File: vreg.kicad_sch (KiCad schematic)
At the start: 24 parts, among them IC9 LTC3113, J5 MMCX-P-P-H-ST-TH1

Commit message: name change to Loriques
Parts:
- C10, C11, C24, C69, C75: symbol autonode:CAP0402 -> Loriques:CAP0402
- C28, C32: symbol autonode:CAP -> Loriques:CAP
- C33, C38: symbol autonode:CAP0603 -> Loriques:CAP0603
- C41, C45, C46: symbol autonode:CAP1206 -> Loriques:CAP1206
- COVER0: footprint autonode:NOTHING -> Loriques:NOTHING; symbol autonode:BULLET -> Loriques:BULLET
- FL1: footprint autonode:YFF31HC2A104MT000N -> Loriques:YFF31HC2A104MT000N; symbol autonode:YFF31HC2A104MT000N -> Loriques:YFF31HC2A104MT000N
- IC9: footprint autonode:SON50P400X500X80-17T244X434N -> Loriques:SON50P400X500X80-17T244X434N; symbol autonode:LTC3113 -> Loriques:LTC3113
- J5: footprint autonode:MMCX-P-P-H-ST-TH1 -> Loriques:MMCX-P-P-H-ST-TH1; symbol autonode:MMCX-P-P-H-ST-TH1 -> Loriques:MMCX-P-P-H-ST-TH1
- L1: footprint autonode:HCMA0703-2R2-R -> Loriques:HCMA0703-2R2-R; symbol autonode:HCMA0703-2R2-R -> Loriques:HCMA0703-2R2-R
- R3, R34, R35, R39, R6, R7: symbol autonode:RESISTOR0402-RES -> Loriques:RESISTOR0402-RES
- S1: footprint autonode:MS288-10F -> Loriques:MS288-10F; symbol autonode:MS288-10F -> Loriques:MS288-10F
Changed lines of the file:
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@@
 	)
 	(symbol
-		(lib_id "autonode:CAP1206")
+		(lib_id "Loriques:CAP1206")
 		(at 88.9 104.14 0)
 		(unit 1)
@@
 		)
 		(instances
-			(project "AutoNode"
+			(project "Loriques"
 				(path "/23714a9e-6212-41ed-9d80-e983f828d45f/a02f1723-ba56-4604-a65b-8dc913c22eb2"
 					(reference "C46")
@@
 	)
 	(symbol
-		(lib_id "autonode:RESISTOR0402-RES")
+		(lib_id "Loriques:RESISTOR0402-RES")
 		(at 256.54 83.82 90)
 		(unit 1)
@@
 		)
 		(instances
-			(project "AutoNode"
+			(project "Loriques"
 				(path "/23714a9e-6212-41ed-9d80-e983f828d45f/a02f1723-ba56-4604-a65b-8dc913c22eb2"
 					(reference "R6")
@@
 	)
 	(symbol
-		(lib_id "autonode:CAP0402")
+		(lib_id "Loriques:CAP0402")
 		(at 228.6 78.74 0)
 		(unit 1)
@@
 		)
 		(instances
-			(project "AutoNode"
+			(project "Loriques"
 				(path "/23714a9e-6212-41ed-9d80-e983f828d45f/a02f1723-ba56-4604-a65b-8dc913c22eb2"
 					(reference "C10")
@@
 	)
 	(symbol
-		(lib_id "autonode:RESISTOR0402-RES")
+		(lib_id "Loriques:RESISTOR0402-RES")
 		(at 170.18 93.98 90)
 		(unit 1)
@@
 		)
 		(instances
-			(project "AutoNode"
+			(project "Loriques"
 				(path "/23714a9e-6212-41ed-9d80-e983f828d45f/a02f1723-ba56-4604-a65b-8dc913c22eb2"
 					(reference "R39")
@@
 	)
 	(symbol
-		(lib_id "autonode:YFF31HC2A104MT000N")
+		(lib_id "Loriques:YFF31HC2A104MT000N")
 		(at 50.8 86.36 0)
 		(unit 1)
@@
 			)
 		)
-		(property "Footprint" "autonode:YFF31HC2A104MT000N"
+		(property "Footprint" "Loriques:YFF31HC2A104MT000N"
 			(at 50.8 86.36 0)
 			(effects
@@
 		)
 		(instances
-			(project "AutoNode"
+			(project "Loriques"
 				(path "/23714a9e-6212-41ed-9d80-e983f828d45f/a02f1723-ba56-4604-a65b-8dc913c22eb2"
 					(reference "FL1")
@@
 	)
 	(symbol
-		(lib_id "autonode:CAP")
+		(lib_id "Loriques:CAP")
 		(at 142.24 104.14 0)
 		(unit 1)
@@
 		)
 		(instances
-			(project "AutoNode"
+			(project "Loriques"
 				(path "/23714a9e-6212-41ed-9d80-e983f828d45f/a02f1723-ba56-4604-a65b-8dc913c22eb2"
 					(reference "C28")
@@
 	)
 	(symbol
-		(lib_id "autonode:CAP0402")
+		(lib_id "Loriques:CAP0402")
 		(at 246.38 101.6 90)
 		(unit 1)
@@
 		)
 		(instances
-			(project "AutoNode"
+			(project "Loriques"
 				(path "/23714a9e-6212-41ed-9d80-e983f828d45f/a02f1723-ba56-4604-a65b-8dc913c22eb2"
 					(reference "C24")
@@
 	)
 	(symbol
-		(lib_id "autonode:CAP0402")
+		(lib_id "Loriques:CAP0402")
 		(at 132.08 104.14 0)
 		(unit 1)
@@
 		)
 		(instances
-			(project "AutoNode"
+			(project "Loriques"
 				(path "/23714a9e-6212-41ed-9d80-e983f828d45f/a02f1723-ba56-4604-a65b-8dc913c22eb2"
 					(reference "C75")
@@
 	)
 	(symbol
-		(lib_id "autonode:BULLET")
+		(lib_id "Loriques:BULLET")
 		(at 284.48 134.62 0)
 		(unit 1)
@@
 			)
 		)
-		(property "Footprint" "autonode:NOTHING"
+		(property "Footprint" "Loriques:NOTHING"
 			(at 284.48 134.62 0)
 			(effects
@@
 		)
 		(instances
-			(project "AutoNode"
+			(project "Loriques"
 				(path "/23714a9e-6212-41ed-9d80-e983f828d45f/a02f1723-ba56-4604-a65b-8dc913c22eb2"
 					(reference "COVER0")
@@
 	)
 	(symbol
-		(lib_id "autonode:MMCX-P-P-H-ST-TH1")
+		(lib_id "Loriques:MMCX-P-P-H-ST-TH1")
 		(at 27.94 99.06 0)
 		(unit 1)
@@
 			)
 		)
-		(property "Footprint" "autonode:MMCX-P-P-H-ST-TH1"
+		(property "Footprint" "Loriques:MMCX-P-P-H-ST-TH1"
 			(at 27.94 99.06 0)
 			(effects
@@
 		)
 		(instances
-			(project "AutoNode"
+			(project "Loriques"
 				(path "/23714a9e-6212-41ed-9d80-e983f828d45f/a02f1723-ba56-4604-a65b-8dc913c22eb2"
 					(reference "J5")
@@
 	)
 	(symbol
-		(lib_id "autonode:LTC3113")
+		(lib_id "Loriques:LTC3113")
 		(at 198.12 96.52 0)
 		(unit 1)
@@
 			)
 		)
-		(property "Footprint" "autonode:SON50P400X500X80-17T244X434N"
+		(property "Footprint" "Loriques:SON50P400X500X80-17T244X434N"
 			(at 197.866 114.554 0)
 			(effects
@@
 		)
 		(instances
-			(project "AutoNode"
+			(project "Loriques"
 				(path "/23714a9e-6212-41ed-9d80-e983f828d45f/a02f1723-ba56-4604-a65b-8dc913c22eb2"
 					(reference "IC9")
@@
 	)
 	(symbol
-		(lib_id "autonode:HCMA0703-2R2-R")
+		(lib_id "Loriques:HCMA0703-2R2-R")
 		(at 198.12 76.2 0)
 		(unit 1)
@@
 			)
 		)
-		(property "Footprint" "autonode:HCMA0703-2R2-R"
+		(property "Footprint" "Loriques:HCMA0703-2R2-R"
 			(at 198.12 76.2 0)
 			(effects
@@
 		)
 		(instances
-			(project "AutoNode"
+			(project "Loriques"
 				(path "/23714a9e-6212-41ed-9d80-e983f828d45f/a02f1723-ba56-4604-a65b-8dc913c22eb2"
 					(reference "L1")
@@
 	)
 	(symbol
-		(lib_id "autonode:CAP0603")
+		(lib_id "Loriques:CAP0603")
 		(at 287.02 96.52 0)
 		(unit 1)
@@
 		)
 		(instances
-			(project "AutoNode"
+			(project "Loriques"
 				(path "/23714a9e-6212-41ed-9d80-e983f828d45f/a02f1723-ba56-4604-a65b-8dc913c22eb2"
 					(reference "C38")
@@
 	)
 	(symbol
-		(lib_id "autonode:RESISTOR0402-RES")
+		(lib_id "Loriques:RESISTOR0402-RES")
 		(at 228.6 88.9 90)
 		(unit 1)
@@
 		)
 		(instances
-			(project "AutoNode"
+			(project "Loriques"
 				(path "/23714a9e-6212-41ed-9d80-e983f828d45f/a02f1723-ba56-4604-a65b-8dc913c22eb2"
 					(reference "R3")
@@
 	)
 	(symbol
-		(lib_id "autonode:RESISTOR0402-RES")
+		(lib_id "Loriques:RESISTOR0402-RES")
 		(at 180.34 114.3 90)
 		(unit 1)
@@
 		)
 		(instances
-			(project "AutoNode"
+			(project "Loriques"
 				(path "/23714a9e-6212-41ed-9d80-e983f828d45f/a02f1723-ba56-4604-a65b-8dc913c22eb2"
 					(reference "R34")
@@
 	)
 	(symbol
-		(lib_id "autonode:CAP1206")
+		(lib_id "Loriques:CAP1206")
 		(at 63.5 104.14 0)
 		(unit 1)
@@
 		)
 		(instances
-			(project "AutoNode"
+			(project "Loriques"
 				(path "/23714a9e-6212-41ed-9d80-e983f828d45f/a02f1723-ba56-4604-a65b-8dc913c22eb2"
 					(reference "C41")
@@
 	)
 	(symbol
-		(lib_id "autonode:RESISTOR0402-RES")
+		(lib_id "Loriques:RESISTOR0402-RES")
 		(at 223.52 101.6 180)
 		(unit 1)
@@
 		)
 		(instances
-			(project "AutoNode"
+			(project "Loriques"
 				(path "/23714a9e-6212-41ed-9d80-e983f828d45f/a02f1723-ba56-4604-a65b-8dc913c22eb2"
 					(reference "R7")
@@
 	)
 	(symbol
-		(lib_id "autonode:MS288-10F")
+		(lib_id "Loriques:MS288-10F")
 		(at 294.64 127 180)
 		(unit 1)
@@
 			)
 		)
-		(property "Footprint" "autonode:MS288-10F"
+		(property "Footprint" "Loriques:MS288-10F"
 			(at 294.64 127 0)
 			(effects
@@
 		)
 		(instances
-			(project "AutoNode"
+			(project "Loriques"
 				(path "/23714a9e-6212-41ed-9d80-e983f828d45f/a02f1723-ba56-4604-a65b-8dc913c22eb2"
 					(reference "S1")
@@
 	)
 	(symbol
-		(lib_id "autonode:CAP0402")
+		(lib_id "Loriques:CAP0402")
 		(at 236.22 106.68 90)
 		(unit 1)
@@
 		)
 		(instances
-			(project "AutoNode"
+			(project "Loriques"
 				(path "/23714a9e-6212-41ed-9d80-e983f828d45f/a02f1723-ba56-4604-a65b-8dc913c22eb2"
 					(reference "C11")
@@
 	)
 	(symbol
-		(lib_id "autonode:CAP0402")
+		(lib_id "Loriques:CAP0402")
 		(at 101.6 104.14 0)
 		(unit 1)
@@
 		)
 		(instances
-			(project "AutoNode"
+			(project "Loriques"
 				(path "/23714a9e-6212-41ed-9d80-e983f828d45f/a02f1723-ba56-4604-a65b-8dc913c22eb2"
 					(reference "C69")
@@
 	)
 	(symbol
-		(lib_id "autonode:CAP")
+		(lib_id "Loriques:CAP")
 		(at 266.7 96.52 0)
 		(unit 1)
@@
 		)
 		(instances
-			(project "AutoNode"
+			(project "Loriques"
 				(path "/23714a9e-6212-41ed-9d80-e983f828d45f/a02f1723-ba56-4604-a65b-8dc913c22eb2"
 					(reference "C32")
@@
 	)
 	(symbol
-		(lib_id "autonode:RESISTOR0402-RES")
+		(lib_id "Loriques:RESISTOR0402-RES")
 		(at 256.54 114.3 90)
 		(unit 1)
@@
 		)
 		(instances
-			(project "AutoNode"
+			(project "Loriques"
 				(path "/23714a9e-6212-41ed-9d80-e983f828d45f/a02f1723-ba56-4604-a65b-8dc913c22eb2"
 					(reference "R35")
@@
 	)
 	(symbol
-		(lib_id "autonode:CAP1206")
+		(lib_id "Loriques:CAP1206")
 		(at 76.2 104.14 0)
 		(unit 1)
@@
 		)
 		(instances
-			(project "AutoNode"
+			(project "Loriques"
 				(path "/23714a9e-6212-41ed-9d80-e983f828d45f/a02f1723-ba56-4604-a65b-8dc913c22eb2"
 					(reference "C45")
@@
 	)
 	(symbol
-		(lib_id "autonode:CAP0603")
+		(lib_id "Loriques:CAP0603")
 		(at 160.02 104.14 0)
 		(unit 1)
@@
 		)
 		(instances
-			(project "AutoNode"
+			(project "Loriques"
 				(path "/23714a9e-6212-41ed-9d80-e983f828d45f/a02f1723-ba56-4604-a65b-8dc913c22eb2"
 					(reference "C33")

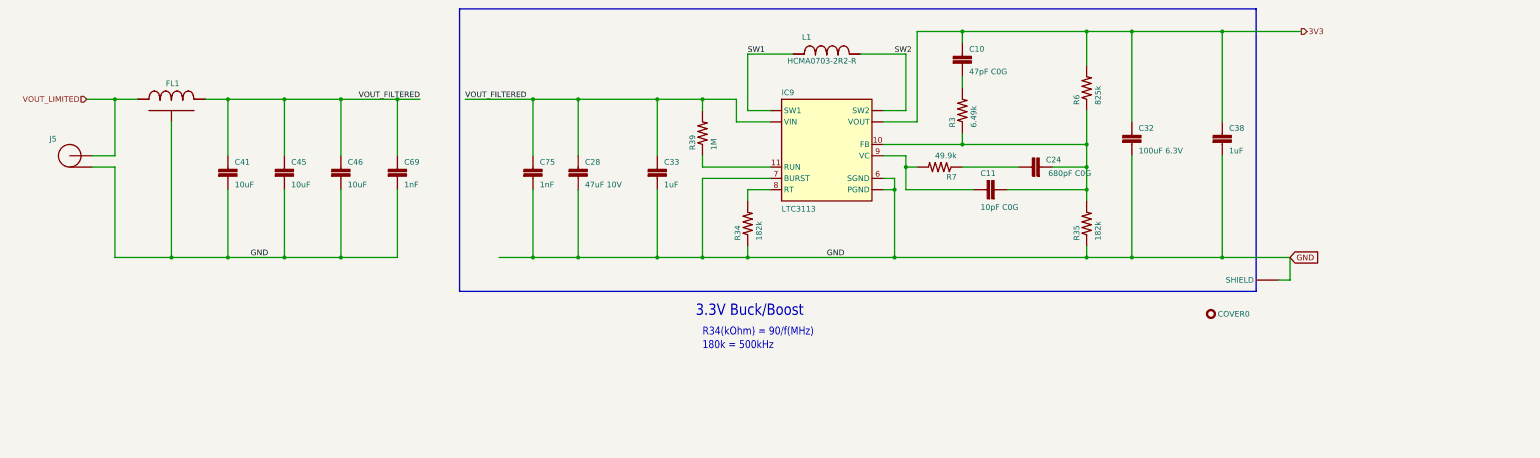
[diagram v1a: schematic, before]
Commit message: added logo to schematic sheets
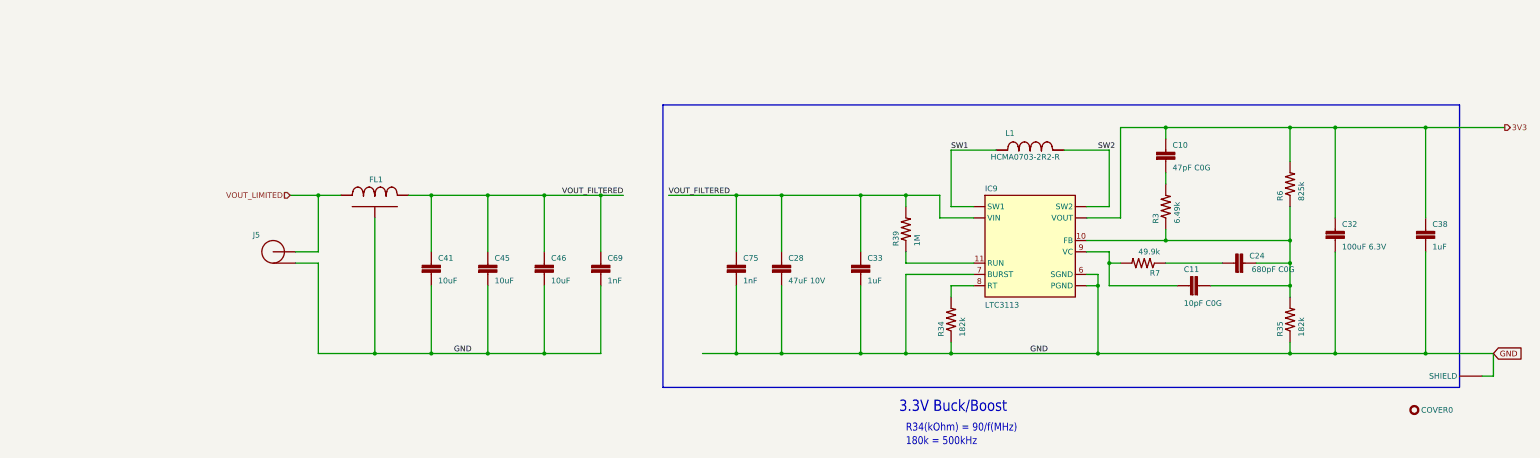
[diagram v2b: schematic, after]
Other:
- title: (none) -> Loriques
- moved on the sheet: C10, C11, C24, C28, C32, C33, C38, C41, C45, C46, C69, C75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

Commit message: lots of routing, tweaking placement. adding courtyards
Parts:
- removed J5: MMCX-P-P-H-ST-TH1, Loriques:MMCX-P-P-H-ST-TH1, symbol Loriques:MMCX-P-P-H-ST-TH1
- L1: value HCMA0703-2R2-R -> 2.2uH; footprint Loriques:HCMA0703-2R2-R -> Loriques:IND_IHLP-2525CZ_VIS; symbol Loriques:HCMA0703-2R2-R -> Device:L; DK (none) -> 541-IHLP2525CZER2R2MA1CT-ND; PARTNO (none) -> IHLP2525CZER2R2MA1
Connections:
- net SW1: now also L1.1; no longer L1.P$1 (1)
- net SW2: now also L1.2; no longer L1.P$2 (2)
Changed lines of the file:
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@@
-	)
-	(junction
-		(at 83.82 107.95)
-		(diameter 0)
-		(color 0 0 0 0)
 	)
 	(junction
@@
 	)
 	(junction
-		(at 96.52 143.51)
-		(diameter 0)
-		(color 0 0 0 0)
-	)
-	(junction
 		(at 332.74 143.51)
 		(diameter 0)
@@
 	(wire
 		(pts
+			(xy 247.65 97.79) (xy 261.62 97.79)
+		)
+		(stroke
+			(width 0.1524)
+			(type solid)
+		)
+	)
+	(wire
+		(pts
 			(xy 347.98 148.59) (xy 347.98 143.51)
 		)
@@
 	(wire
 		(pts
-			(xy 83.82 120.65) (xy 83.82 107.95)
-		)
-		(stroke
-			(width 0.1524)
-			(type solid)
-		)
-	)
-	(wire
-		(pts
 			(xy 223.52 113.03) (xy 223.52 107.95)
 		)
@@
 	(wire
 		(pts
-			(xy 83.82 123.19) (xy 83.82 143.51)
-		)
-		(stroke
-			(width 0.1524)
-			(type solid)
-		)
-	)
-	(wire
-		(pts
 			(xy 302.26 100.33) (xy 302.26 92.71)
 		)
@@
 	(wire
 		(pts
-			(xy 261.62 97.79) (xy 251.46 97.79)
-		)
-		(stroke
-			(width 0.1524)
-			(type solid)
-		)
-	)
-	(wire
-		(pts
 			(xy 302.26 143.51) (xy 259.08 143.51)
 		)
@@
 	(wire
 		(pts
-			(xy 83.82 107.95) (xy 88.9 107.95)
-		)
-		(stroke
-			(width 0.1524)
-			(type solid)
-		)
-	)
-	(wire
-		(pts
 			(xy 177.8 143.51) (xy 187.96 143.51)
 		)
@@
 	(wire
 		(pts
-			(xy 78.74 120.65) (xy 83.82 120.65)
-		)
-		(stroke
-			(width 0.1524)
-			(type solid)
-		)
-	)
-	(wire
-		(pts
 			(xy 264.16 113.03) (xy 264.16 92.71)
 		)
@@
 	(wire
 		(pts
-			(xy 78.74 123.19) (xy 83.82 123.19)
-		)
-		(stroke
-			(width 0.1524)
-			(type solid)
-		)
-	)
-	(wire
-		(pts
-			(xy 177.8 128.27) (xy 177.8 143.51)
-		)
-		(stroke
-			(width 0.1524)
-			(type solid)
-		)
-	)
-	(wire
-		(pts
-			(xy 134.62 107.95) (xy 147.32 107.95)
-		)
-		(stroke
-			(width 0.1524)
-			(type solid)
-		)
-	)
-	(wire
-		(pts
-			(xy 332.74 143.51) (xy 312.42 143.51)
-		)
-		(stroke
-			(width 0.1524)
-			(type solid)
-		)
-	)
-	(wire
-		(pts
-			(xy 77.47 107.95) (xy 83.82 107.95)
+			(xy 236.22 97.79) (xy 240.03 97.79)
 		)
 		(stroke
@@
 	(wire
 		(pts
+			(xy 177.8 128.27) (xy 177.8 143.51)
+		)
+		(stroke
+			(width 0.1524)
+			(type solid)
+		)
+	)
+	(wire
+		(pts
+			(xy 134.62 107.95) (xy 147.32 107.95)
+		)
+		(stroke
+			(width 0.1524)
+			(type solid)
+		)
+	)
+	(wire
+		(pts
+			(xy 332.74 143.51) (xy 312.42 143.51)
+		)
+		(stroke
+			(width 0.1524)
+			(type solid)
+		)
+	)
+	(wire
+		(pts
+			(xy 77.47 107.95) (xy 88.9 107.95)
+		)
+		(stroke
+			(width 0)
+			(type default)
+		)
+	)
+	(wire
+		(pts
 			(xy 134.62 128.27) (xy 134.62 143.51)
 		)
@@
 		(pts
 			(xy 134.62 120.65) (xy 134.62 107.95)
-		)
-		(stroke
-			(width 0.1524)
-			(type solid)
-		)
-	)
-	(wire
-		(pts
-			(xy 83.82 143.51) (xy 96.52 143.51)
 		)
 		(stroke
@@
 	)
 	(symbol
-		(lib_id "Loriques:MMCX-P-P-H-ST-TH1")
-		(at 73.66 120.65 0)
-		(unit 1)
-		(exclude_from_sim no)
-		(in_bom yes)
-		(on_board yes)
-		(dnp no)
-		(property "Reference" "J5"
-			(at 69.088 117.602 0)
-			(effects
-				(font
-					(size 1.27 1.27)
-				)
-				(justify left bottom)
-			)
-		)
-		(property "Value" "MMCX-P-P-H-ST-TH1"
-			(at 73.66 120.65 0)
-			(effects
-				(font
-					(size 1.27 1.27)
-				)
-				(hide yes)
-			)
-		)
-		(property "Footprint" "Loriques:MMCX-P-P-H-ST-TH1"
-			(at 73.66 120.65 0)
-			(effects
-				(font
-					(size 1.27 1.27)
-				)
-				(hide yes)
-			)
-		)
-		(property "Datasheet" ""
-			(at 73.66 120.65 0)
-			(effects
-				(font
-					(size 1.27 1.27)
-				)
-				(hide yes)
-			)
-		)
-		(property "Description" "MMCX Connector Plug, Male Pin 50Ohm Through Hole Solder"
-			(at 73.66 120.65 0)
-			(effects
-				(font
-					(size 1.27 1.27)
-				)
-				(hide yes)
-			)
-		)
-		(property "DNP" "T"
-			(at 73.66 120.65 0)
-			(effects
-				(font
-					(size 1.27 1.27)
-				)
-				(justify left bottom)
-				(hide yes)
-			)
-		)
-		(pin "P$1"
-		)
-		(pin "P$2"
-		)
-		(pin "P$3"
-		)
-		(pin "P$4"
-		)
-		(pin "PIN"
-		)
-		(instances
-			(project "Loriques"
-				(path "/23714a9e-6212-41ed-9d80-e983f828d45f/a02f1723-ba56-4604-a65b-8dc913c22eb2"
-					(reference "J5")
-					(unit 1)
-				)
-			)
-		)
-	)
-	(symbol
 		(lib_id "Loriques:LTC3113")
 		(at 243.84 118.11 0)
@@
 	)
 	(symbol
-		(lib_id "Loriques:HCMA0703-2R2-R")
-		(at 243.84 97.79 0)
+		(lib_id "Device:L")
+		(at 243.84 97.79 90)
 		(unit 1)
 		(exclude_from_sim no)
@@
 		(dnp no)
 		(property "Reference" "L1"
-			(at 238.252 94.742 0)
-			(effects
-				(font
-					(size 1.27 1.27)
-				)
-				(justify left bottom)
-			)
-		)
-		(property "Value" "HCMA0703-2R2-R"
-			(at 234.95 100.076 0)
-			(effects
-				(font
-					(size 1.27 1.27)
-				)
-				(justify left bottom)
-			)
-		)
-		(property "Footprint" "Loriques:HCMA0703-2R2-R"
+			(at 244.856 94.742 90)
+			(effects
+				(font
+					(size 1.27 1.27)
+				)
+				(justify left bottom)
+			)
+		)
+		(property "Value" "2.2uH"
+			(at 246.634 98.552 90)
+			(effects
+				(font
+					(size 1.27 1.27)
+				)
+				(justify left bottom)
+			)
+		)
+		(property "Footprint" "Loriques:IND_IHLP-2525CZ_VIS"
 			(at 243.84 97.79 0)
 			(effects
@@
 			)
 		)
-		(property "Datasheet" ""
+		(property "Datasheet" "~"
 			(at 243.84 97.79 0)
 			(effects
@@
 			)
 		)
-		(property "Description" "2.2µH Shielded Wirewound Inductor 8A 20mOhm Max Nonstandard"
+		(property "Description" "Inductor"
 			(at 243.84 97.79 0)
 			(effects
@@
 			)
 		)
-		(pin "P$1"
-		)
-		(pin "P$2"
+		(property "PARTNO" "IHLP2525CZER2R2MA1"
+			(at 243.84 97.79 0)
+			(effects
+				(font
+					(size 1.27 1.27)
+				)
+				(hide yes)
+			)
+		)
+		(property "DK" "541-IHLP2525CZER2R2MA1CT-ND"
+			(at 243.84 97.79 0)
+			(effects
+				(font
+					(size 1.27 1.27)
+				)
+				(hide yes)
+			)
+		)
+		(pin "1"
+		)
+		(pin "2"
 		)
 		(instances

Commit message: initial routing done!
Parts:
- IC9: DK (none) -> LTC3113IDHD#TRPBFCT-ND; PARTNO (none) -> LTC3113IDHD#TRPBF
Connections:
- net GND: no longer IC9.P$1 (PGND), IC9.P$2 (PGND), IC9.P$3 (PGND), IC9.P$4 (PGND), IC9.P$5 (PGND), IC9.P$6 (PGND)
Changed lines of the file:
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@@
 			)
 		)
-		(property "Datasheet" ""
+		(property "Datasheet" "https://www.analog.com/media/en/technical-documentation/data-sheets/3113f.pdf"
 			(at 243.84 118.11 0)
 			(effects
@@
 		(property "Description" "Buck-Boost Switching Regulator IC Positive Adjustable 1.8V 1 Output 3A 16-WFDFN Exposed Pad"
 			(at 245.618 138.43 0)
+			(effects
+				(font
+					(size 1.27 1.27)
+				)
+				(hide yes)
+			)
+		)
+		(property "PARTNO" "LTC3113IDHD#TRPBF"
+			(at 243.586 141.732 0)
+			(effects
+				(font
+					(size 1.27 1.27)
+				)
+				(hide yes)
+			)
+		)
+		(property "DK" "LTC3113IDHD#TRPBFCT-ND"
+			(at 243.586 141.732 0)
 			(effects
 				(font
@@
 		(pin "9"
 		)
-		(pin "P$1"
-		)
-		(pin "P$2"
-		)
-		(pin "P$3"
-		)
-		(pin "P$4"
-		)
-		(pin "P$5"
-		)
-		(pin "P$6"
-		)
 		(pin "1"
